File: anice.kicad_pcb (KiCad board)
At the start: 4 copper layers, 65 x 40 mm, 83 parts, among them J1 Conn_02x20_Counter_Clockwise, J2 Micro_SD_Card_Det1, J3 USB_C_Receptacle_USB2.0_14P, J4 USB_C_Receptacle_USB2.0_14P, J5 USB_C_Receptacle_USB2.0_14P, J6 CONN_02X03, J7 HDMI_C_1.3, U1 ECP5U_12_CABGA256, U10 W9825G6KH-6, U11 W25Q128JVS, U2 TLV62569DBV, U3 TLV62569DBV, U4 TLV62569DBV, U5 USBLC6-2P6, U6 USBLC6-2P6, U7 FT231XQ, U8 USBLC6-2P6, U9 PCA9306DC1, Y1 ECS-2520MV-xxx-xx

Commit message: Add a gitignore
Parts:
- moved U11 11.9 mm to (123.5, 81.5), turned to -90 degrees
- moved H1 4.00 mm to (105.5, 72.5)
- moved J1 4.00 mm to (110.4, 73.8)
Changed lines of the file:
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@@
 				(vias not_allowed)
 				(pads not_allowed)
-				(copperpour allowed)
+				(copperpour not_allowed)
 				(footprints allowed)
 			)
@@
 	(footprint "Connector_PinHeader_2.54mm:PinHeader_2x20_P2.54mm_Vertical"
 		(layer "F.Cu")
-		(at 110.375 69.775 90)
+		(at 110.375 73.775 90)
 		(descr "Through hole straight pin header, 2x20, 2.54mm pitch, double rows")
 		(tags "Through hole pin header THT 2x20 2.54mm double row")
@@
 	(footprint "MountingHole:MountingHole_2.5mm"
 		(layer "F.Cu")
-		(at 105.5 68.5)
+		(at 105.5 72.5)
 		(descr "Mounting Hole 2.5mm, no annular")
 		(tags "mounting hole 2.5mm no annular")
@@
 	(footprint "Package_SO:SOIC-8_5.3x5.3mm_P1.27mm"
 		(layer "F.Cu")
-		(at 134.23 76.43 180)
+		(at 123.5 81.5 -90)
 		(descr "SOIC, 8 Pin (JEITA/EIAJ 08-001-BBA and Atmel/Microchip, 208 mils width, https://www.jeita.or.jp/japanese/standard/book/ED-7311-19/#target/page_no=21, https://ww1.microchip.com/downloads/en/DeviceDoc/20005045C.pdf#page=23, https://ww1.microchip.com/downloads/en/DeviceDoc/doc2535.pdf#page=162), generated with kicad-footprint-generator ipc_gullwing_generator.py")
 		(tags "SOIC SO P-SOP SOP SOP-8 SO SO-8 8S2 S2AE/F K04-056 CASE-751BE SO8W 8-Pin-SOIC PSA W8-2 W8-4 W8MS-1")
 		(property "Reference" "U11"
-			(at 0 -3.6 0)
+			(at 0 -3.6 90)
 			(layer "F.SilkS")
 			(effects
@@
 		)
 		(property "Value" "W25Q128JVS"
-			(at 0 3.6 0)
+			(at 0 3.6 90)
 			(layer "F.Fab")
 			(effects
@@
 		)
 		(property "Datasheet" "https://www.winbond.com/resource-files/w25q128jv_dtr%20revc%2003272018%20plus.pdf"
-			(at 0 0 0)
+			(at 0 0 90)
 			(layer "F.Fab")
 			(hide yes)
@@
 		)
 		(property "Description" "128Mbit / 16MiB Serial Flash Memory, Standard/Dual/Quad SPI, 2.7-3.6V, SOIC-8"
-			(at 0 0 0)
+			(at 0 0 90)
 			(layer "F.Fab")
 			(hide yes)
@@
 		)
 		(property "LCSC Part" " C97521"
-			(at 0 0 180)
+			(at 0 0 270)
 			(unlocked yes)
 			(layer "F.Fab")
@@
 		(attr smd)
 		(fp_line
-			(start 2.76 2.76)
-			(end 2.76 2.49)
+			(start -2.76 2.76)
+			(end -2.76 2.49)
 			(stroke
 				(width 0.12)
@@
 		)
 		(fp_line
-			(start 2.76 -2.76)
-			(end 2.76 -2.49)
+			(start 0 2.76)
+			(end -2.76 2.76)
 			(stroke
 				(width 0.12)
@@
 		)
 		(fp_line
-			(start 0 2.76)
-			(end -2.76 2.76)
+			(start 2.76 2.76)
+			(end 2.76 2.49)
 			(stroke
 				(width 0.12)
@@
 		)
 		(fp_line
-			(start 0 -2.76)
-			(end 2.76 -2.76)
+			(start -2.76 -2.76)
+			(end -2.76 -2.49)
 			(stroke
 				(width 0.12)
@@
 		)
 		(fp_line
-			(start -2.76 2.76)
-			(end -2.76 2.49)
+			(start 0 -2.76)
+			(end 2.76 -2.76)
 			(stroke
 				(width 0.12)
@@
 		)
 		(fp_line
-			(start -2.76 -2.76)
-			(end -2.76 -2.49)
+			(start 2.76 -2.76)
+			(end 2.76 -2.49)
 			(stroke
 				(width 0.12)
@@
 		)
 		(fp_line
-			(start 2.65 2.65)
-			(end -2.65 2.65)
+			(start -2.65 2.65)
+			(end -2.65 -1.65)
 			(stroke
 				(width 0.1)
@@
 		)
 		(fp_line
-			(start 2.65 -2.65)
-			(end 2.65 2.65)
+			(start 2.65 2.65)
+			(end -2.65 2.65)
 			(stroke
 				(width 0.1)
@@
 		)
 		(fp_line
-			(start -1.65 -2.65)
-			(end 2.65 -2.65)
+			(start -2.65 -1.65)
+			(end -1.65 -2.65)
 			(stroke
 				(width 0.1)
@@
 		)
 		(fp_line
-			(start -2.65 2.65)
-			(end -2.65 -1.65)
+			(start -1.65 -2.65)
+			(end 2.65 -2.65)
 			(stroke
 				(width 0.1)
@@
 		)
 		(fp_line
-			(start -2.65 -1.65)
-			(end -1.65 -2.65)
+			(start 2.65 -2.65)
+			(end 2.65 2.65)
 			(stroke
 				(width 0.1)
@@
 		)
 		(fp_text user "${REFERENCE}"
-			(at 0 0 0)
+			(at 0 0 90)
 			(layer "F.Fab")
 			(effects
@@
 		)
 		(pad "1" smd roundrect
-			(at -3.5875 -1.905 180)
+			(at -3.5875 -1.905 270)
 			(size 1.625 0.65)
 			(layers "F.Cu" "F.Mask" "F.Paste")
@@
 		)
 		(pad "2" smd roundrect
-			(at -3.5875 -0.635 180)
+			(at -3.5875 -0.635 270)
 			(size 1.625 0.65)
 			(layers "F.Cu" "F.Mask" "F.Paste")
@@
 		)
 		(pad "3" smd roundrect
-			(at -3.5875 0.635 180)
+			(at -3.5875 0.635 270)
 			(size 1.625 0.65)
 			(layers "F.Cu" "F.Mask" "F.Paste")
@@
 		)
 		(pad "4" smd roundrect
-			(at -3.5875 1.905 180)
+			(at -3.5875 1.905 270)
 			(size 1.625 0.65)
 			(layers "F.Cu" "F.Mask" "F.Paste")
@@
 		)
 		(pad "5" smd roundrect
-			(at 3.5875 1.905 180)
+			(at 3.5875 1.905 270)
 			(size 1.625 0.65)
 			(layers "F.Cu" "F.Mask" "F.Paste")
@@
 		)
 		(pad "6" smd roundrect
-			(at 3.5875 0.635 180)
+			(at 3.5875 0.635 270)
 			(size 1.625 0.65)
 			(layers "F.Cu" "F.Mask" "F.Paste")
@@
 		)
 		(pad "7" smd roundrect
-			(at 3.5875 -0.635 180)
+			(at 3.5875 -0.635 270)
 			(size 1.625 0.65)
 			(layers "F.Cu" "F.Mask" "F.Paste")
@@
 		)
 		(pad "8" smd roundrect
-			(at 3.5875 -1.905 180)
+			(at 3.5875 -1.905 270)
 			(size 1.625 0.65)
 			(layers "F.Cu" "F.Mask" "F.Paste")
@@
 	)
 	(segment
-		(start 103.21 91.025)
-		(end 103.21 90.02)
-		(width 0.2)
-		(layer "F.Cu")
-		(net 140)
-	)
-	(segment
 		(start 146.6 98.15)
 		(end 147.14 98.15)
@@
 	)
 	(segment
+		(start 103.21 91.025)
+		(end 104.475 91.025)
+		(width 0.2)
+		(layer "F.Cu")
+		(net 140)
+	)
+	(segment
+		(start 104.475 91.025)
+		(end 104.5 91)
+		(width 0.2)
+		(layer "F.Cu")
+		(net 140)
+	)
+	(segment
 		(start 159.74 98.15)
 		(end 160.32 98.73)
@@
 	)
 	(via
-		(at 103.21 90.02)
+		(at 104.5 91)
 		(size 0.6)
 		(drill 0.3)

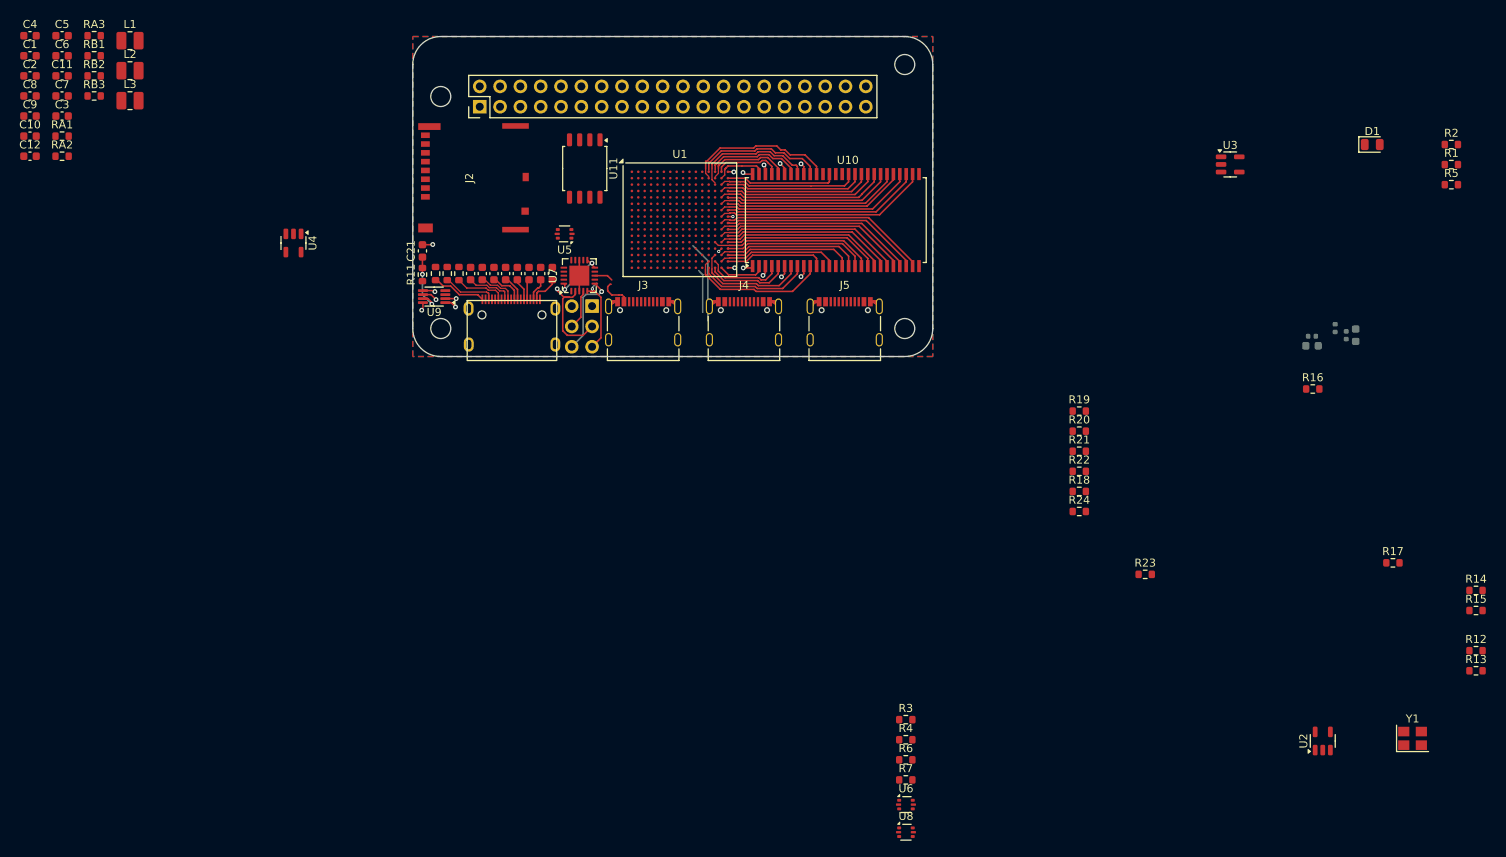
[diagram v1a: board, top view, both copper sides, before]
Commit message: Routed HDMI, usb, rotated chip and more
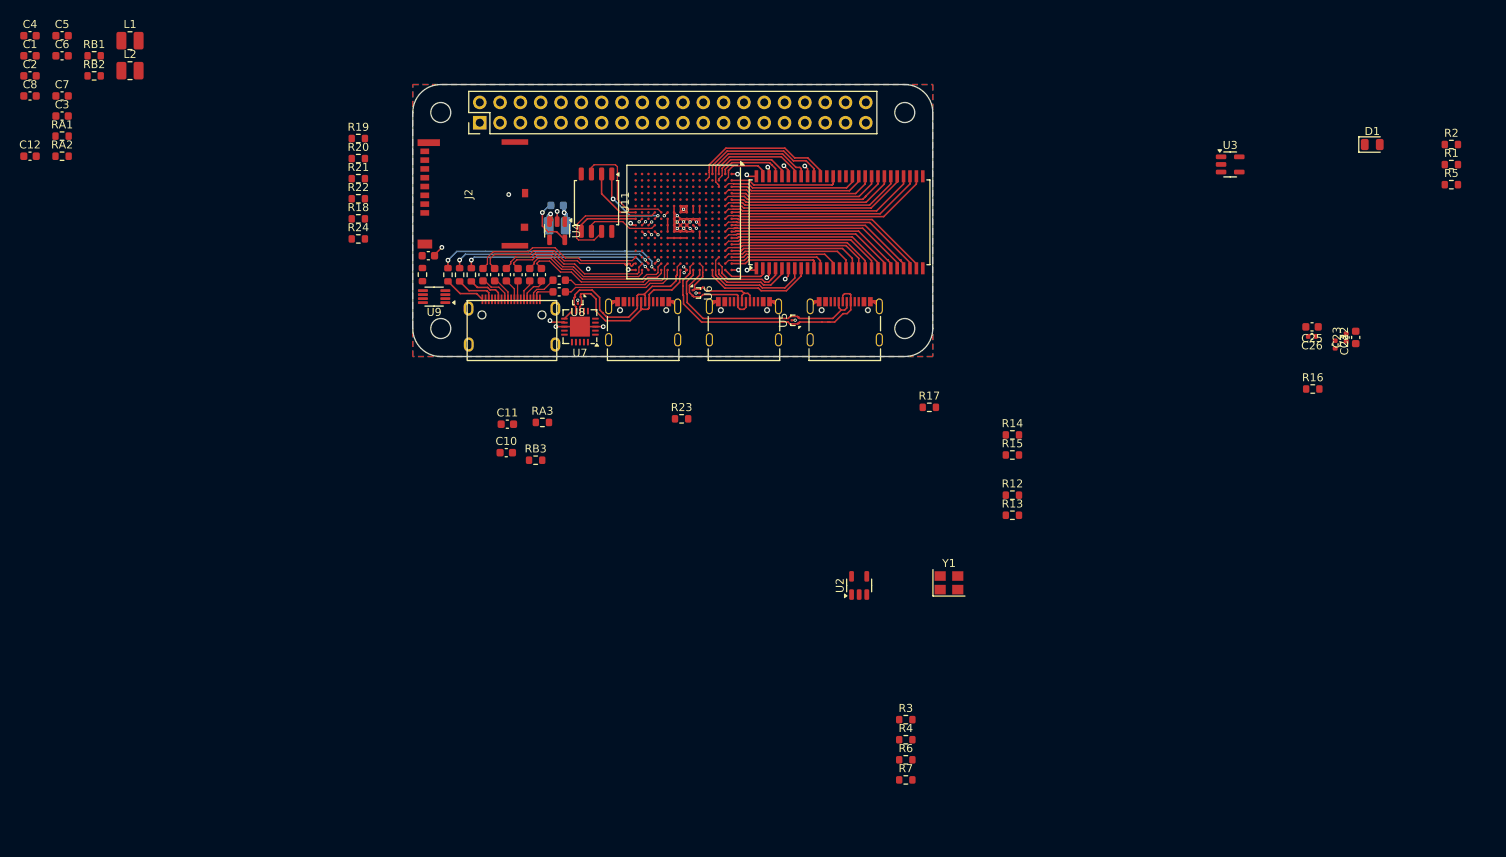
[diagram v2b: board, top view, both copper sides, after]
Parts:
- removed J6: CONN_02X03, Connector_PinHeader_2.54mm:PinHeader_2x03_P2.54mm_Vertical
- C22, C23, C24, C25, C26: moved to F.Cu
- C9, L3: moved to B.Cu
- U5, U6, U8: value USBLC6-2P6 -> TPD2EUSB30; footprint Package_TO_SOT_SMD:SOT-666 -> Package_TO_SOT_SMD:Texas_DRT-3
- moved R18 96.3 mm to (95.2, 87.8)
- moved R19 96.3 mm to (95.2, 77.8)
- moved R20 96.3 mm to (95.2, 80.3)
- moved R21 96.3 mm to (95.2, 82.8)
- moved R22 96.3 mm to (95.2, 85.3)
- moved R24 96.3 mm to (95.2, 90.3)
- moved U8 78.1 mm to (122.6, 98.0), turned to 180 degrees
- moved RA3 74.0 mm to (118.2, 113.2)
- moved RB3 71.5 mm to (117.4, 118.0)
- moved C10 71.5 mm to (113.7, 117.0)
- moved C11 70.7 mm to (113.8, 113.5)
- moved U6 69.1 mm to (137.4, 97.1), turned to -90 degrees
- moved C9 66.8 mm to (120.0, 86.1), turned to 180 degrees
- moved R17 61.1 mm to (166.6, 111.3)
- moved R23 61.1 mm to (135.6, 112.8)
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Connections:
- J3 pad A6: Net-(J3-D+-PadA6) -> D1+
- J3 pad A7: Net-(J3-D--PadA7) -> D1-
- J3 pad B6: Net-(J3-D+-PadA6) -> D1+
- J3 pad B7: Net-(J3-D--PadA7) -> D1-
- J4 pad A6: Net-(J4-D+-PadA6) -> D2+
- J4 pad A7: Net-(J4-D--PadA7) -> D2-
- J4 pad B6: Net-(J4-D+-PadA6) -> D2+
- J4 pad B7: Net-(J4-D--PadA7) -> D2-
- J5 pad A6: Net-(J5-D+-PadA6) -> D3+
- J5 pad A7: Net-(J5-D--PadA7) -> D3-
- J5 pad B6: Net-(J5-D+-PadA6) -> D3+
- J5 pad B7: Net-(J5-D--PadA7) -> D3-
- U1 pad A10: unconnected-(U1C-PT42B/--PadA10) -> SDRAM_A10
- U1 pad A11: unconnected-(U1C-PT53A/+-PadA11) -> SDRAM_BA0
- U1 pad A12: unconnected-(U1C-PT53B/--PadA12) -> SDRAM_nRAS
- U1 pad A13: SDRAM_D10 -> SDRAM_nWE
- U1 pad A14: SDRAM_D12 -> SDRAM_D7
- U1 pad A15: SDRAM_D14 -> SDRAM_D5
- U1 pad A2: unconnected-(U1B-PT4A/+-PadA2) -> SDRAM_D8
- U1 pad A3: unconnected-(U1B-PT6A/+-PadA3) -> SDRAM_CLK
- U1 pad A4: unconnected-(U1B-PT6B/--PadA4) -> SDRAM_A12
- U1 pad A5: unconnected-(U1B-PT18A/+-PadA5) -> SDRAM_A9
- U1 pad A6: unconnected-(U1B-PT18B/--PadA6) -> SDRAM_A7
- U1 pad A7: unconnected-(U1B-PT29A/+/PCLKT0_0-PadA7) -> SDRAM_A5
- U1 pad A8: unconnected-(U1B-PT29B/-/PCLKC0_0-PadA8) -> SDRAM_A3
- U1 pad A9: unconnected-(U1C-PT42A/+-PadA9) -> SDRAM_A1
- U1 pad B1: unconnected-(U1G-PL2A/+/HS/LDQ8-PadB1) -> SDRAM_D14
- U1 pad B10: unconnected-(U1C-PT44A/+-PadB10) -> SDRAM_A0
- U1 pad B11: unconnected-(U1C-PT49A/+-PadB11) -> SDRAM_BA1
- U1 pad B12: unconnected-(U1C-PT56A/+-PadB12) -> SDRAM_nCS
- U1 pad B13: SDRAM_D9 -> SDRAM_nCAS
- U1 pad B14: SDRAM_D13 -> SDRAM_DQM0
- U1 pad B15: SDRAM_D15 -> SDRAM_D6
- U1 pad B16: SDRAM_D8 -> SDRAM_D0
- U1 pad B2: unconnected-(U1G-PL2B/-/HS/LDQ8-PadB2) -> SDRAM_D15
- U1 pad B3: unconnected-(U1B-PT4B/--PadB3) -> SDRAM_DQM1
- U1 pad B4: unconnected-(U1B-PT11B/--PadB4) -> SDRAM_CKE
- U1 pad B5: unconnected-(U1B-PT15B/--PadB5) -> SDRAM_A11
- U1 pad B6: unconnected-(U1B-PT22B/--PadB6) -> SDRAM_A8
- U1 pad B7: unconnected-(U1B-PT27B/-/PCLKC0_1-PadB7) -> SDRAM_A6
- U1 pad B8: unconnected-(U1C-PT35B/-/PCLKC1_0-PadB8) -> SDRAM_A4
- U1 pad B9: unconnected-(U1C-PT38A/+/GR_PCLK1_0-PadB9) -> SDRAM_A2
- U1 pad C1: unconnected-(U1G-PL5A/+/HS/LDQ8-PadC1) -> SDRAM_D12
- U1 pad C14: SDRAM_D11 -> SDRAM_D3
- U1 pad C15: SDRAM_DQM1 -> SDRAM_D1
- U1 pad C16: SDRAM_CLK -> SDRAM_D2
- U1 pad C2: unconnected-(U1G-PL5B/-/HS/LDQ8-PadC2) -> SDRAM_D13
- U1 pad C3: unconnected-(U1G-PL2C/+/LDQ8-PadC3) -> SDRAM_D11
- U1 pad D1: unconnected-(U1G-PL8A/+/HS/LDQS8-PadD1) -> SDRAM_D10
- U1 pad D16: SDRAM_A12 -> SDRAM_D4
- U1 pad E15: SDRAM_A11 -> unconnected-(U1D-PR8B/-/HS/RDQSN8-PadE15)
- U1 pad E16: SDRAM_A9 -> unconnected-(U1D-PR11D/-/RDQ8-PadE16)
- U1 pad E2: unconnected-(U1G-PL8B/-/HS/LDQSN8-PadE2) -> SDRAM_D9
- U1 pad F15: SDRAM_A8 -> D2+
- U1 pad F16: SDRAM_A7 -> D2-
- U1 pad G15: SDRAM_A6 -> D3+
- U1 pad G16: SDRAM_A5 -> D3-
- U1 pad H15: SDRAM_A4 -> unconnected-(U1D-PR20B/-/HS/RDQSN20-PadH15)
- U1 pad J15: SDRAM_A3 -> D1-
- U1 pad J16: SDRAM_A2 -> D1+
- U1 pad K15: SDRAM_A1 -> unconnected-(U1D-PR23D/-/PCLKC2_0/RDQ20-PadK15)
- U1 pad K16: SDRAM_A0 -> unconnected-(U1D-PR23C/+/PCLKT2_0/RDQ20-PadK16)
- U1 pad L15: SDRAM_A10 -> FPDI_D2-
- U1 pad L16: SDRAM_BA1 -> FPDI_D2+
- U1 pad M14: SDRAM_nRAS -> unconnected-(U1E-PR32D/-/RDQ32-PadM14)
- U1 pad M15: SDRAM_BA0 -> FPDI_D1-
- U1 pad M16: SDRAM_nCS -> FPDI_D1+
- U1 pad N16: SDRAM_nCAS -> FPDI_HPD
- U1 pad P14: SDRAM_D3 -> unconnected-(U1E-PR38B/-/HS/RDQ44-PadP14)
- U1 pad P15: SDRAM_nWE -> FPDI_UTIL
- U1 pad P16: SDRAM_DQM0 -> FPDI_CEC
- U1 pad R13: SDRAM_D5 -> unconnected-(U1E-PR41C/+/RDQ44-PadR13)
- U1 pad R14: SDRAM_D1 -> unconnected-(U1E-PR41B/-/HS/RDQ44-PadR14)
- U1 pad R15: SDRAM_D7 -> FPDI_D0-
- U1 pad R16: SDRAM_D6 -> FPDI_D0+
- U1 pad T13: SDRAM_D4 -> unconnected-(U1E-PR44B/-/HS/RDQSN44-PadT13)
- U1 pad T14: SDRAM_D2 -> FPDI_CLK-
- U1 pad T15: SDRAM_D0 -> FPDI_CLK+
- U5 pad 1: Net-(J3-D--PadA7) -> D3+
- U5 pad 2: GND -> D3-
- U5 pad 3: Net-(J3-D+-PadA6) -> GND
- U6 pad 1: Net-(J4-D--PadA7) -> D2+
- U6 pad 2: GND -> D2-
- U6 pad 3: Net-(J4-D+-PadA6) -> GND
- U7 pad 8: Net-(U7-USBDP) -> D1+
- U7 pad 9: Net-(U7-USBDM) -> D1-
- U8 pad 1: Net-(J5-D--PadA7) -> D1+
- U8 pad 2: GND -> D1-
- U8 pad 3: Net-(J5-D+-PadA6) -> GND
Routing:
- net D3+: track 0.00 -> 32.1 mm
- net FPDI_HPD: track 0.00 -> 28.9 mm, vias 0 -> 2
- net D3-: track 0.00 -> 27.9 mm
- net FPDI_UTIL: track 0.00 -> 25.4 mm, vias 0 -> 2
- net FPDI_CEC: track 0.00 -> 24.0 mm, vias 0 -> 2
- net D1-: track 0.00 -> 23.6 mm
- net D1+: track 0.00 -> 23.3 mm
- net FPDI_CLK-: track 0.00 -> 21.5 mm
- net FPDI_CLK+: track 0.00 -> 21.4 mm
- net FPDI_D0-: track 0.00 -> 19.9 mm
- net GND: track 33.1 -> 52.9 mm, vias 10 -> 29
- net FPDI_D1-: track 0.00 -> 19.4 mm
- net FPDI_D0+: track 0.00 -> 19.0 mm
- net FPDI_D1+: track 0.00 -> 18.5 mm
- net IO3: track 0.00 -> 15.8 mm
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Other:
- board size 65 x 40 mm -> 65 x 34 mm

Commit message: Stash
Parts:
- removed C1, C22: 10uF, Capacitor_SMD:C_0603_1608Metric
- removed C24: 100nF, Capacitor_SMD:C_0402_1005Metric
- removed C5: 100pF, Capacitor_SMD:C_0603_1608Metric
- removed C6: 22uF, Capacitor_SMD:C_0603_1608Metric
- removed C7: 2.2uF, Capacitor_SMD:C_0603_1608Metric
- removed U2, U3, U4: TLV62569DBV, Package_TO_SOT_SMD:SOT-23-5
- added C27: 100pF, Capacitor_SMD:C_0603_1608Metric, F.Cu at (118.4, 84.8)
- added C28: 10uF, Capacitor_SMD:C_0603_1608Metric, F.Cu at (152.9, 79.7)
- added C29: 100pF, Capacitor_SMD:C_0603_1608Metric, F.Cu at (152.9, 78.3)
- added C30: 10uF, Capacitor_SMD:C_0603_1608Metric, B.Cu at (139.4, 87.2)
- added C31: 100nF, Capacitor_SMD:C_0402_1005Metric, B.Cu at (138.2, 85.9)
- added C32: 10uF, Capacitor_SMD:C_0603_1608Metric, B.Cu at (140.1, 90.1)
- added C33: 100nF, Capacitor_SMD:C_0402_1005Metric, B.Cu at (138.9, 89.6)
- added C34: 100nF, Capacitor_SMD:C_0402_1005Metric, B.Cu at (138.9, 91.4)
- added C35: 100nF, Capacitor_SMD:C_0402_1005Metric, B.Cu at (138.3, 87.7)
- added C36: 100nF, Capacitor_SMD:C_0402_1005Metric, B.Cu at (137.6, 91.1)
- added C37: 100nF, Capacitor_SMD:C_0402_1005Metric, B.Cu at (137.3, 85.4)
- added C38: 100nF, Capacitor_SMD:C_0402_1005Metric, B.Cu at (136.7, 87.8)
- added C39: 100nF, Capacitor_SMD:C_0402_1005Metric, F.Cu at (123.2, 91.4)
- added C40: 15pF, Capacitor_SMD:C_0402_1005Metric, B.Cu at (127.0, 92.5)
- added C41: 100nF, Capacitor_SMD:C_0402_1005Metric, B.Cu at (130.7, 89.0)
- added C42: 100nF, Capacitor_SMD:C_0402_1005Metric, B.Cu at (134.9, 89.7)
- added U12: TLV62569DRL, Package_TO_SOT_SMD:SOT-563, F.Cu at (118.2, 90.2)
- added U13: TLV62569DRL, Package_TO_SOT_SMD:SOT-563, F.Cu at (120.3, 80.9)
- added U14: TLV62569DRL, Package_TO_SOT_SMD:SOT-563, F.Cu at (160.3, 78.5)
- C10: value 22uF -> 100pF
- C11: value 2.2uF -> 10uF
- C12, C4, C8: value 22uF -> 10uF
- C2: value 22uF -> 10uF; moved to B.Cu
- C23, C25, C26, R1, R12, R13, R14, R15, R16, R17, R18, R19, R2, R22, R23, R3, R4: moved to B.Cu
- C3: value 2.2uF -> 10uF; moved to B.Cu
- C9: value 100pF -> 10uF; moved to F.Cu
- D1: footprint LED_SMD:LED_0805_2012Metric -> LED_SMD:LED_0603_1608Metric
- J3, J4, J5: footprint Connector_USB:USB_C_Receptacle_Palconn_UTC16-G -> Connector_USB:USB_C_Receptacle_GCT_USB4105-xx-A_16P_TopMnt_Horizontal
- L3: moved to F.Cu
- moved C4 109.5 mm to (162.8, 78.8), turned to -90 degrees
- moved R1 103.6 mm to (129.5, 97.7), turned to -90 degrees
- moved R2 101.0 mm to (133.2, 100.1), turned to 180 degrees
- moved RA1 100.2 mm to (158.4, 80.0), turned to 90 degrees
- moved RB1 99.2 mm to (160.6, 80.2), turned to 180 degrees
- moved R5 96.4 mm to (136.9, 100.3), turned to -90 degrees
- moved L1 90.7 mm to (156.3, 79.5), turned to -90 degrees
- moved R16 89.0 mm to (128.1, 87.8), turned to -90 degrees
- moved D1 88.6 mm to (136.8, 103.3), turned to -90 degrees
- moved C23 84.8 mm to (134.6, 91.4), turned to 135 degrees
- moved C2 83.3 mm to (136.1, 84.9), turned to 90 degrees
- moved C26 83.1 mm to (132.9, 85.9), turned to 0 degrees
- moved C25 82.7 mm to (133.4, 84.7), turned to 0 degrees
- moved C3 80.1 mm to (136.5, 91.9), turned to -90 degrees
- moved R15 74.9 mm to (105.3, 95.4), turned to 180 degrees
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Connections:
- C11 pad 1: +3V3 -> +2V5
- C9 pad 2: /Power/FB3 -> GND
- J1 pad 10: unconnected-(J1-Pin_10-Pad10) -> CONN10
- J1 pad 11: unconnected-(J1-Pin_11-Pad11) -> CONN11
- J1 pad 12: unconnected-(J1-Pin_12-Pad12) -> CONN12
- J1 pad 13: unconnected-(J1-Pin_13-Pad13) -> CONN13
- J1 pad 15: unconnected-(J1-Pin_15-Pad15) -> CONN15
- J1 pad 16: unconnected-(J1-Pin_16-Pad16) -> CONN16
- J1 pad 18: unconnected-(J1-Pin_18-Pad18) -> CONN18
- J1 pad 19: unconnected-(J1-Pin_19-Pad19) -> CONN19
- J1 pad 21: unconnected-(J1-Pin_21-Pad21) -> CONN21
- J1 pad 22: unconnected-(J1-Pin_22-Pad22) -> CONN22
- J1 pad 23: unconnected-(J1-Pin_23-Pad23) -> CONN23
- J1 pad 24: unconnected-(J1-Pin_24-Pad24) -> CONN24
- J1 pad 26: unconnected-(J1-Pin_26-Pad26) -> CONN26
- J1 pad 27: unconnected-(J1-Pin_27-Pad27) -> CONN27
- J1 pad 28: unconnected-(J1-Pin_28-Pad28) -> CONN28
- J1 pad 29: unconnected-(J1-Pin_29-Pad29) -> CONN29
- J1 pad 3: unconnected-(J1-Pin_3-Pad3) -> CONN3
- J1 pad 31: unconnected-(J1-Pin_31-Pad31) -> CONN31
- J1 pad 32: unconnected-(J1-Pin_32-Pad32) -> CONN32
- J1 pad 33: unconnected-(J1-Pin_33-Pad33) -> CONN33
- J1 pad 35: unconnected-(J1-Pin_35-Pad35) -> CONN35
- J1 pad 36: unconnected-(J1-Pin_36-Pad36) -> CONN36
- J1 pad 37: unconnected-(J1-Pin_37-Pad37) -> CONN37
- J1 pad 38: unconnected-(J1-Pin_38-Pad38) -> CONN38
- J1 pad 40: unconnected-(J1-Pin_40-Pad40) -> CONN40
- J1 pad 5: unconnected-(J1-Pin_5-Pad5) -> CONN5
- J1 pad 7: unconnected-(J1-Pin_7-Pad7) -> CONN7
- J1 pad 8: unconnected-(J1-Pin_8-Pad8) -> CONN8
- R14 pad 1: +2V5 -> +3V3
- R15 pad 1: +2V5 -> +3V3
- U1 pad E1: unconnected-(U1G-PL11D/-/LDQ8-PadE1) -> CONN40
- U1 pad E3: unconnected-(U1G-PL5C/+/LDQ8-PadE3) -> CONN37
- U1 pad F1: unconnected-(U1G-PL14A/+/HS/LDQ20-PadF1) -> CONN35
- U1 pad K13: unconnected-(U1E-PR29A/+/GR_PCLK3_0/HS/RDQ32-PadK13) -> GCLK
- U1 pad P5: unconnected-(U1F-PL47D/-/LLC_GPLL0C_IN/LDQ44-PadP5) -> FPDI_SDA
- U1 pad R1: unconnected-(U1F-PL35B/-/VREF1_6/HS/LDQ32-PadR1) -> CONN15
- U1 pad R2: unconnected-(U1F-PL38C/+/LDQ44-PadR2) -> CONN8
- U1 pad R3: unconnected-(U1F-PL41B/-/HS/LDQ44-PadR3) -> CONN5
- U1 pad R4: unconnected-(U1F-PL41C/+/LDQ44-PadR4) -> FPDI_SCL
- U1 pad T2: unconnected-(U1F-PL38D/-/LDQ44-PadT2) -> CONN7
- U1 pad T3: unconnected-(U1F-PL41D/-/LDQ44-PadT3) -> CONN3
- U9 pad 2: +2V5 -> +3V3
- Y1 pad 1: unconnected-(Y1-Tri-State-Pad1) -> +3V3
- Y1 pad 2: unconnected-(Y1-GND-Pad2) -> GND
- Y1 pad 3: unconnected-(Y1-OUT-Pad3) -> GCLK
- Y1 pad 4: unconnected-(Y1-VDD-Pad4) -> +3V3
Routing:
- net +5V: track 1.91 -> 161.7 mm, vias 1 -> 13
- net +3V3: track 17.4 -> 72.8 mm, vias 7 -> 33
- net +2V5: track 0.60 -> 53.1 mm, vias 1 -> 6
- net +1V1: track 2.95 -> 45.2 mm, vias 1 -> 10
- net FPDI_SDA: track 0.00 -> 39.6 mm, vias 0 -> 2
- net FPDI_SCL: track 0.00 -> 38.2 mm, vias 0 -> 2
- net GND: track 52.9 -> 84.1 mm, vias 29 -> 52
- net JTAG_TDO: track 0.00 -> 26.9 mm, vias 0 -> 2
- net CONN40: track 0.00 -> 26.0 mm
- net CONN37: track 0.00 -> 23.0 mm
- net CONN3: track 0.00 -> 22.7 mm
- net JTAG_TCK: track 0.00 -> 21.0 mm, vias 0 -> 2
- net CONN5: track 0.00 -> 20.9 mm
- net JTAG_TDI: track 0.00 -> 20.5 mm, vias 0 -> 2
- net CONN8: track 0.00 -> 19.4 mm
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- added copper zone on F.Cu, net +1V1
- added copper zone on F.Cu, net +2V5
- added copper zone on F.Cu, net +3V3
- added copper zone on In2.Cu, net +5V
- added copper zone on F.Cu, net /Power/L1
- added copper zone on F.Cu, net /Power/L2
- added copper zone on F.Cu, net /Power/L3
